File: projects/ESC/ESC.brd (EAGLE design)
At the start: 139.7 x 38.1 mm, 93 parts, among them J1 1755529, J2 1755529, J3 1755529, J4 1755529, U1 STM32F405RGT6, U10 CSD88584Q5DCT, U11 CSD88584Q5DCT, U12 CSD88584Q5DCT, U13 CSD88584Q5DCT, U14 SN74CBTLV3257PWR, U15 CSD88584Q5DCT, U16 CSD88584Q5DCT, U17 CSD88584Q5DCT, U2 CSD88584Q5DCT, U3 CSD88584Q5DCT, U4 CSD88584Q5DCT, U8 CSD88584Q5DCT, U9 CSD88584Q5DCT, Y1 ECS-80-S-4X

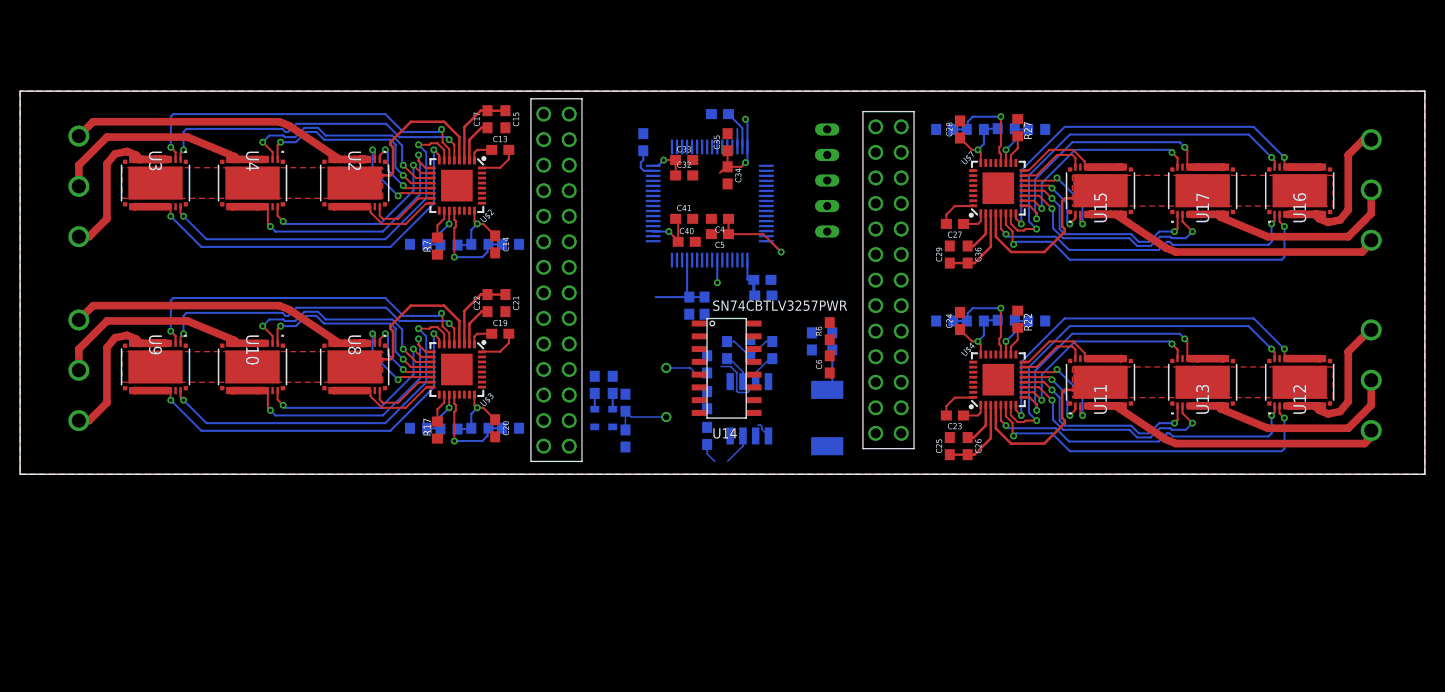
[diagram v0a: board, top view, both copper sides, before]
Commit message: All DRVs connected to STM
now for the fun part...
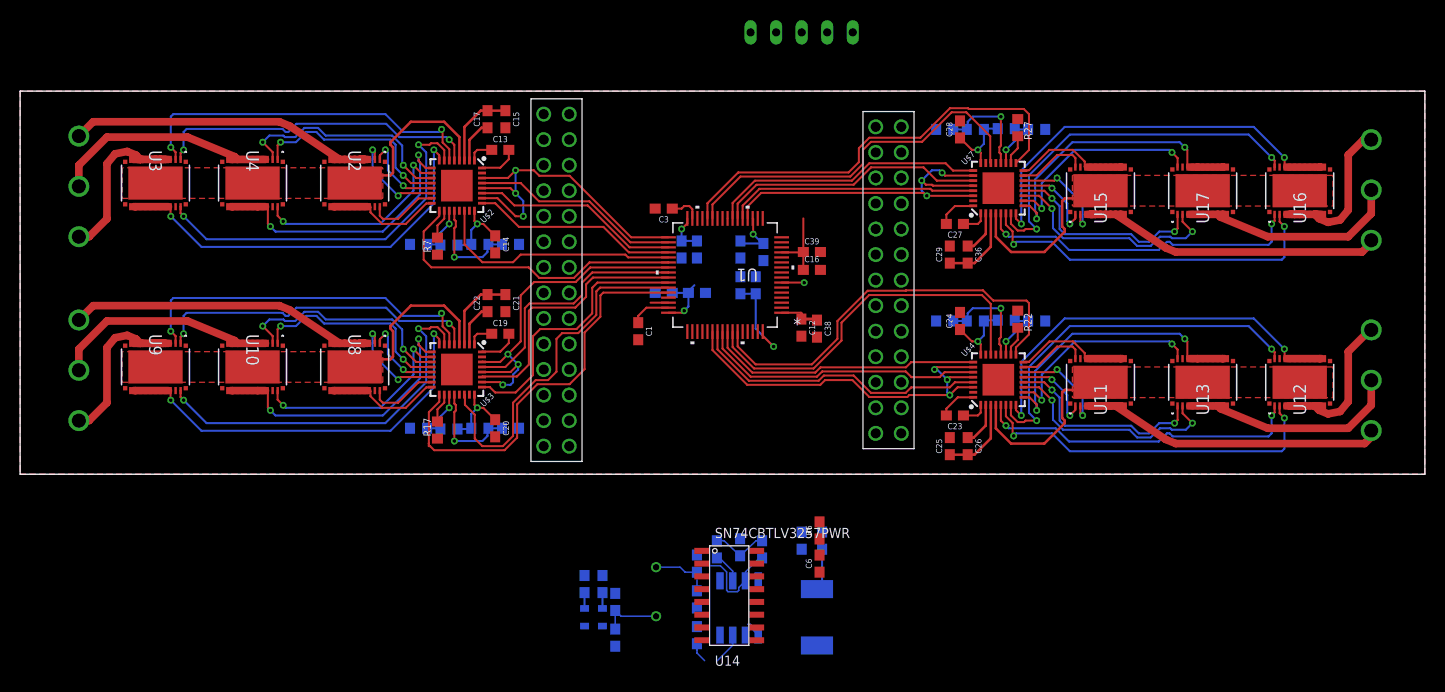
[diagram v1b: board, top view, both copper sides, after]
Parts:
- moved C1 23.1 mm to (61.5, 14.2), flipped to the top, turned to 270 degrees
- moved U14 22.6 mm to (67.8, -7.62)
- moved C10 19.8 mm to (79.8, -6.60)
- moved C2 19.8 mm to (67.3, -8.89)
- moved C6 19.8 mm to (79.5, -8.89)
- moved GREEN_LED 19.8 mm to (57.9, -14.2)
- moved R1 19.8 mm to (57.9, -10.9)
- moved R2 19.8 mm to (56.1, -10.9)
- moved R28 19.8 mm to (73.8, -7.47)
- moved R29 19.8 mm to (69.3, -7.47)
- moved R3 19.8 mm to (59.2, -16.3)
- moved R4 19.8 mm to (77.7, -6.60)
- moved R6 19.8 mm to (79.5, -5.59)
- moved RED_LED 19.8 mm to (56.1, -14.2)
- moved RESET1 19.8 mm to (79.2, -14.2)
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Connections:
- net EN_3: now also U1.58; no longer U1.55
- net FAULT_3: now also U1.59; no longer U1.54
- net INHA_3: now also U1.57; no longer U1.56
- net INHA_4: now also U1.23; no longer U1.50
- net INHB_3: now also U1.56; no longer U1.57
- net INHB_4: now also U1.22; no longer U1.51
- net INHC_3: now also U1.55; no longer U1.59
- net INHC_4: now also U1.21; no longer U1.53
- net INL_3: now also U1.54; no longer U1.58
- net INL_4: now also U1.20; no longer U1.52
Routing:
- net FAULT_4: track 0.04 -> 43.9 mm
- net FAULT_3: track 0.03 -> 41.5 mm
- net FAULT_2: track 0.00 -> 41.4 mm
- net INL_3: track 0.02 -> 40.4 mm, vias 0 -> 3
- net EN_3: track 0.01 -> 37.6 mm
- net EN_4: track 0.03 -> 37.3 mm
- net INL_4: track 0.00 -> 37.1 mm, vias 0 -> 3
- net EN_2: track 0.00 -> 36.1 mm
- net INL_2: track 0.00 -> 35.8 mm, vias 0 -> 3
- net INL_1: track 0.00 -> 34.9 mm, vias 0 -> 3
- net FAULT_1: track 0.03 -> 31.3 mm
- net INHC_3: track 0.03 -> 29.9 mm
- net INHB_3: track 0.01 -> 28.4 mm
- net INHA_3: track 0.01 -> 27.5 mm
- net INHA_4: track 0.00 -> 27.4 mm
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
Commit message: Almost finished quad ESC center
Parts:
- moved C2 49.8 mm to (69.6, 40.9)
- moved C31 48.6 mm to (73.6, 41.2)
- moved R3 48.6 mm to (61.2, 32.3)
- moved C11 48.6 mm to (61.2, 35.8)
- moved C30 48.6 mm to (69.3, 32.5)
- moved GREEN_LED 48.6 mm to (59.9, 34.3)
- moved R1 48.6 mm to (59.9, 37.6)
- moved R2 48.6 mm to (58.2, 37.6)
- moved R28 48.6 mm to (75.8, 41.0)
- moved R29 48.6 mm to (71.3, 41.0)
- moved R5 48.6 mm to (69.3, 36.1)
- moved RED_LED 48.6 mm to (58.2, 34.3)
- moved U$6 48.6 mm to (71.6, 32.5)
- moved Y1 48.6 mm to (65.3, 36.8)
- moved RESET1 19.3 mm to (78.0, 5.08), flipped to the top, turned to 180 degrees
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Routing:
- net NRST: track 6.43 -> 22.6 mm
- net SWDIO: track 1.78 -> 13.2 mm
- net CAN_H: track 9.49 -> 0.00 mm
- net N$7: track 6.16 -> 0.00 mm
- net N$8: track 6.13 -> 0.00 mm
- net N$46: track 5.69 -> 0.00 mm
- net SWCLK: track 0.00 -> 5.44 mm
- net CAN_L: track 3.09 -> 0.00 mm
- net +3V3: track 41.7 -> 38.9 mm
- net N$10: track 0.00 -> 2.26 mm
- net CAN_TX: track 1.65 -> 0.00 mm
- net N$3: track 1.58 -> 0.00 mm
- net N$2: track 1.58 -> 0.00 mm

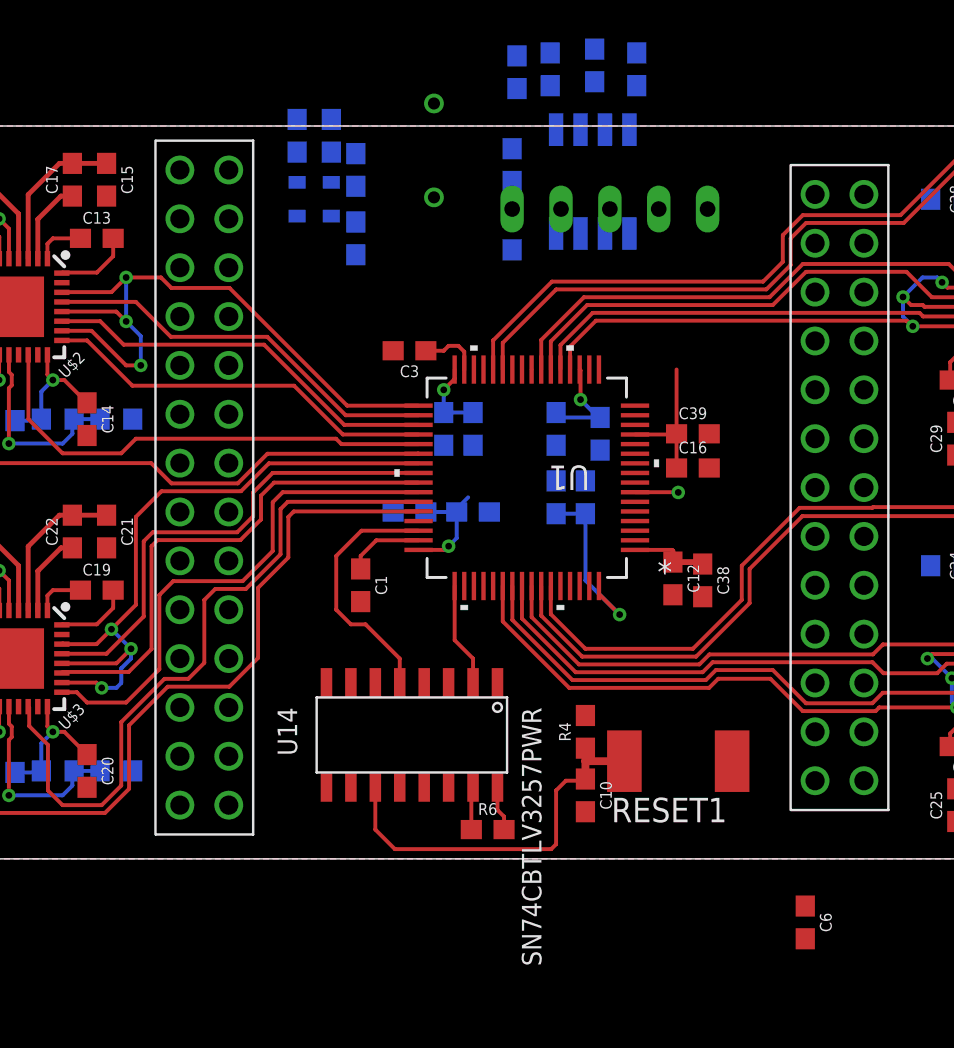
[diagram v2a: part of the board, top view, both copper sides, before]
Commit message: Finished center of quad ESC per the schematic, multiplexer needs revisions.
I routed the airwires, but I believe some are incorrect.
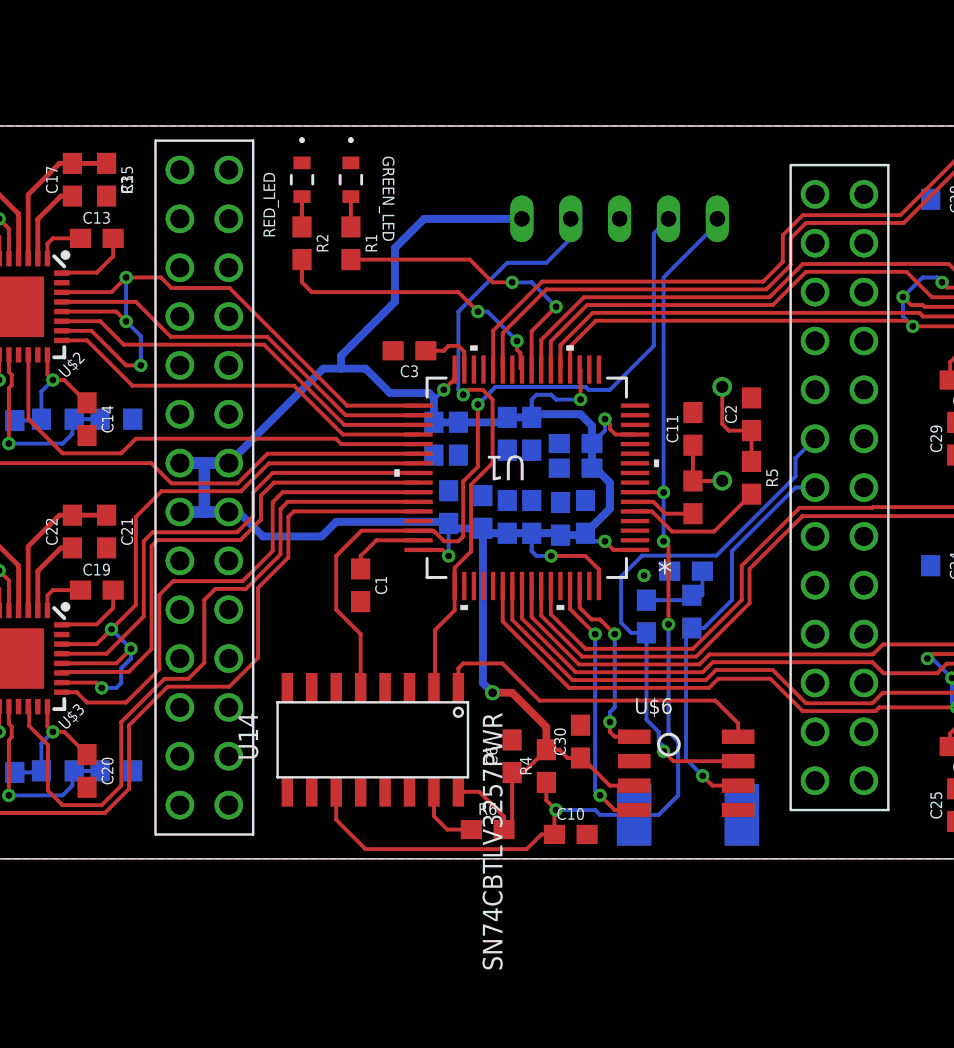
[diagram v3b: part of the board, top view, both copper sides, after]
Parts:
- moved U$6 30.2 mm to (75.7, 2.54), flipped to the top, turned to 0 degrees
- moved R29 29.1 mm to (78.7, 12.9)
- moved R28 28.5 mm to (76.3, 12.6)
- moved C31 26.7 mm to (78.4, 15.0), turned to 180 degrees
- moved C30 26.7 mm to (72.9, 6.10), flipped to the top
- moved C11 22.1 mm to (78.7, 22.4), flipped to the top
- moved R3 22.1 mm to (78.7, 18.8), flipped to the top
- moved C2 21.6 mm to (81.8, 23.1), flipped to the top
- moved Y1 21.0 mm to (80.3, 22.1)
- moved R5 20.5 mm to (81.8, 19.8), flipped to the top
- moved C6 17.5 mm to (69.3, 5.33), turned to 90 degrees
- moved C38 6.93 mm to (73.2, 17.8), flipped to the bottom, turned to 90 degrees
- moved C12 6.61 mm to (71.9, 17.7), flipped to the bottom, turned to 90 degrees
- moved C39 6.12 mm to (72.6, 21.6), flipped to the bottom
- moved C16 6.10 mm to (72.6, 20.3), flipped to the bottom
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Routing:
- net +3V3: track 38.9 -> 123.8 mm, vias 4 -> 7
- net NRST: track 22.6 -> 56.5 mm, vias 1 -> 4
- net CAN_H: track 0.00 -> 28.2 mm, vias 0 -> 1
- net SWDIO: track 13.2 -> 39.5 mm, vias 0 -> 1
- net SWCLK: track 5.44 -> 31.5 mm, vias 0 -> 1
- net CAN_L: track 0.00 -> 21.1 mm, vias 0 -> 1
- net S: track 0.00 -> 17.7 mm
- net N$1: track 0.01 -> 15.5 mm, vias 0 -> 2
- net N$4: track 0.00 -> 15.2 mm, vias 0 -> 2
- net CAN_RX: track 0.00 -> 13.6 mm, vias 0 -> 2
- net CAN_TX: track 0.00 -> 10.1 mm, vias 0 -> 2
- net OSC_IN: track 0.00 -> 7.30 mm
- net N$8: track 0.00 -> 5.20 mm
- net N$46: track 0.00 -> 4.27 mm
- net N$7: track 0.00 -> 3.38 mm
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
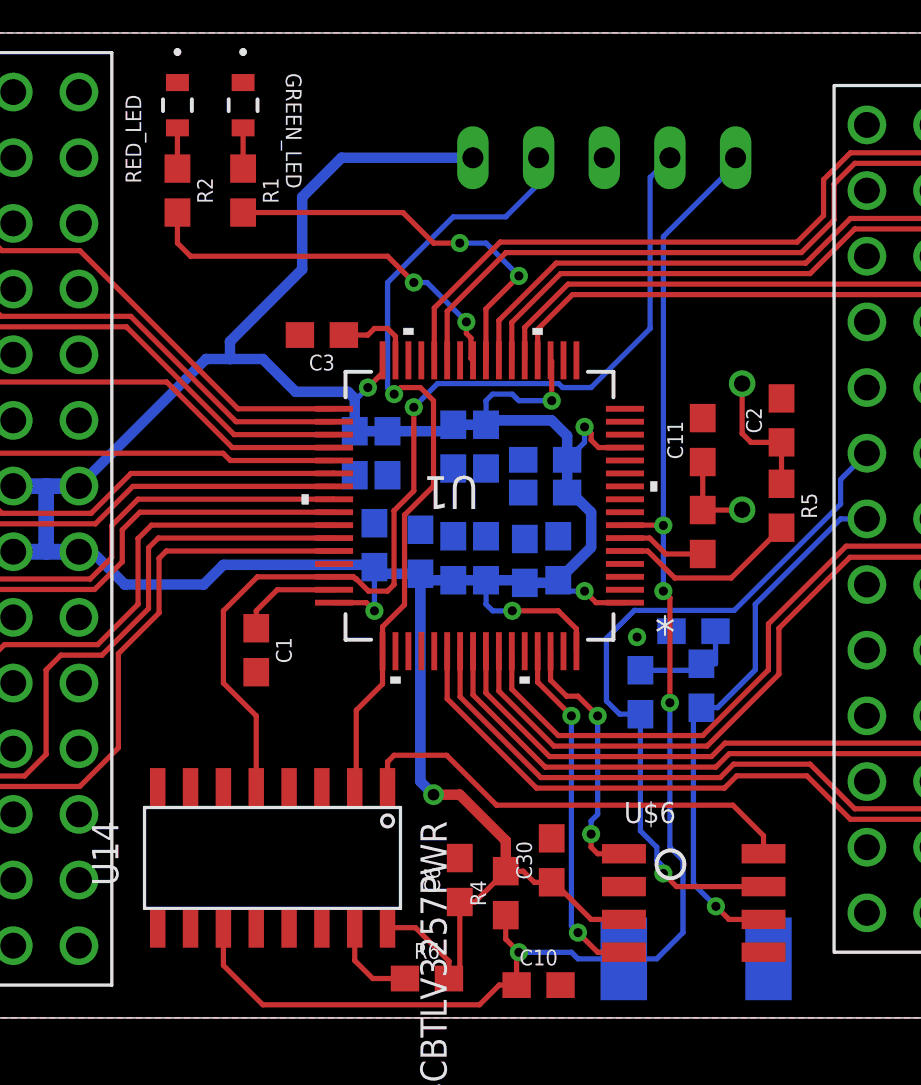
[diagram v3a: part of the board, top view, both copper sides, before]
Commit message: Fixed center and schematics.
"S" on the can tranciever and "S" on the multiplexer are entirely different things. and the multiplexer distinguishes between the can module and the header pin, apparently.
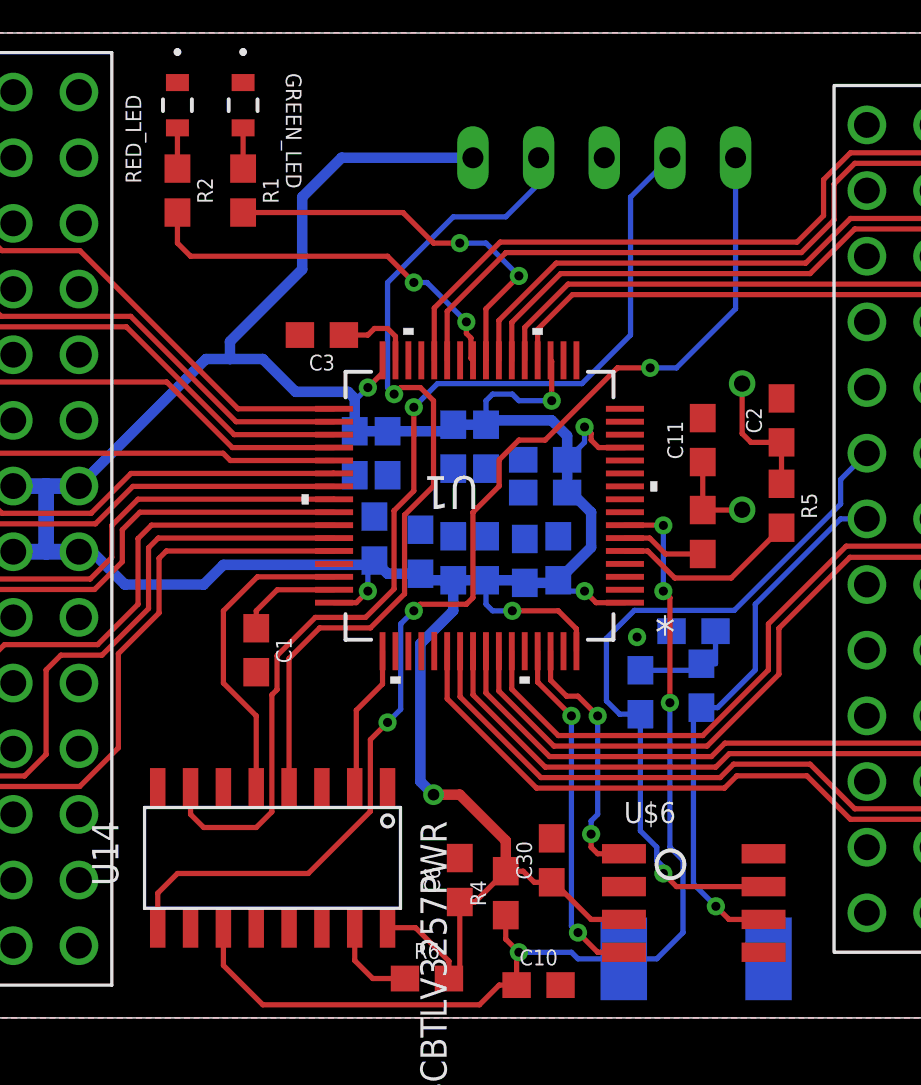
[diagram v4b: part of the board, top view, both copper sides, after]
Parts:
- moved C35 0.25 mm to (66.0, 18.5)
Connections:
- net NRST: no longer SV2.1
- net NRST_IN: now also SV2.1
- net S: no longer U$6.S
- net SWCLK: no longer SV2.4
- net SWCLK_IN: now also SV2.4
- net SWDIO: no longer SV2.2
- net SWDIO_IN: now also SV2.2
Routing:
- net NRST_IN: track 0.00 -> 45.2 mm, vias 0 -> 3
- net SWDIO_IN: track 0.00 -> 40.7 mm, vias 0 -> 1
- net SWCLK_IN: track 0.00 -> 33.7 mm, vias 0 -> 1
- net SWDIO: track 39.5 -> 12.2 mm, vias 1 -> 0
- net SWCLK: track 31.5 -> 5.74 mm, vias 1 -> 0
- net S: track 17.7 -> 0.00 mm
- net NRST: track 56.5 -> 41.1 mm
